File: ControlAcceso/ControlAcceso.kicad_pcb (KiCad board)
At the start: 2 copper layers, 53.3 x 61 mm, 12 parts

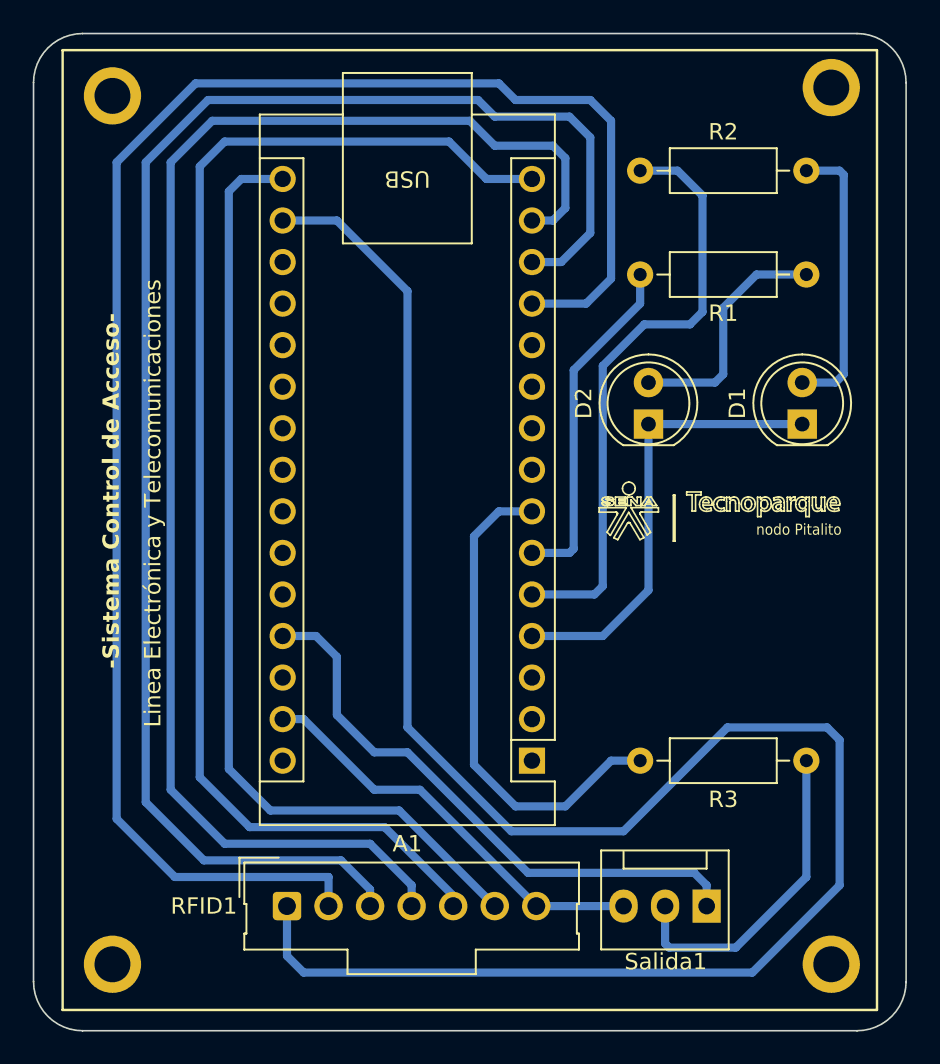
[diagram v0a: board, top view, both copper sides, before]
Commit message: Cambios Significativos
Se quito codigo de prueba, se cambio modulo RFID y se agrego  regulador 7805.
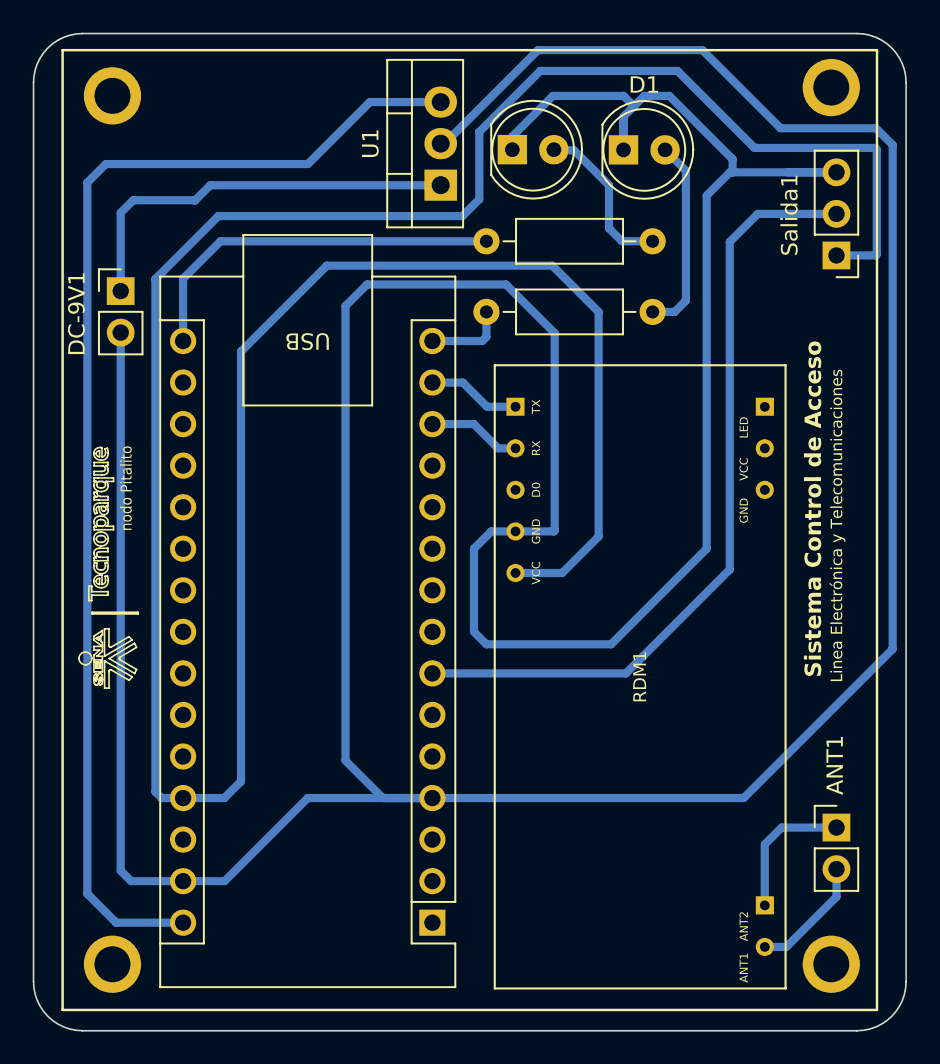
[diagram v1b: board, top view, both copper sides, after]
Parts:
- removed R3: 0, Resistor_THT:R_Axial_DIN0207_L6.3mm_D2.5mm_P10.16mm_Horizontal
- removed RFID1: Conn_01x07, Connector_Molex:Molex_SL_171971-0007_1x07_P2.54mm_Vertical
- added ANT1: Conn_01x02_Pin, Connector_PinHeader_2.54mm:PinHeader_1x02_P2.54mm_Vertical, F.Cu at (242.1, 84.1)
- added DC-9V1: Conn_01x02_Pin, Connector_PinHeader_2.54mm:PinHeader_1x02_P2.54mm_Vertical, F.Cu at (198.4, 51.3)
- added RDM1: RDM6300, RDM6300:RDM6300, F.Cu at (230.1, 74.9)
- added U1: LM7805_TO220, Package_TO_SOT_THT:TO-220-3_Vertical, F.Cu at (217.9, 44.8)
- Salida1: footprint Connector:FanPinHeader_1x03_P2.54mm_Vertical -> Connector_PinHeader_2.54mm:PinHeader_1x03_P2.54mm_Vertical
- moved Salida1 40.6 mm to (242.1, 49.1)
- moved D1 20.0 mm to (229.1, 42.7), turned to 0 degrees
- moved D2 18.7 mm to (222.3, 42.7), turned to 0 degrees
- moved R2 12.8 mm to (220.7, 52.6)
- moved A1 11.6 mm to (217.4, 89.9)
- moved R1 9.62 mm to (230.9, 48.3)
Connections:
- A1 pad 12: RST -> unconnected-(A1-D9-Pad12)
- A1 pad 13: SPI -> TX-SERIAL
- A1 pad 14: MOSI -> RX-SERIAL
- A1 pad 15: MISO -> LED-ON
- A1 pad 16: SCK -> LED-OFF
- A1 pad 5: LED-ON -> unconnected-(A1-D2-Pad5)
- A1 pad 6: LED-OFF -> unconnected-(A1-D3-Pad6)
- Salida1 pad 2: Net-(Salida1-Pin_2) -> OUT
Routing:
- net GND: track 53.4 -> 293.8 mm
- net +5V: track 35.6 -> 171.1 mm
- net 3V3: track 116.4 -> 0.00 mm
- net RST: track 104.6 -> 0.00 mm
- net SPI: track 95.9 -> 0.00 mm
- net MOSI: track 88.3 -> 0.00 mm
- net MISO: track 78.4 -> 0.00 mm
- net VIN: track 0.00 -> 73.5 mm
- net SCK: track 58.6 -> 0.00 mm
- net LED-ON: track 37.0 -> 4.93 mm
- net Net-(DC-9V1-Pin_1): track 0.00 -> 24.9 mm
- net Net-(Salida1-Pin_2): track 19.9 -> 0.00 mm
- net OUT: track 30.5 -> 48.1 mm
- net Net-(ANT1-Pin_1): track 0.00 -> 8.53 mm
- net Net-(ANT1-Pin_2): track 0.00 -> 7.34 mm
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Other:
- board text added: "Sistema Control de Acceso"
- board text removed: "-Sistema Control de Acceso-"

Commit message: Modificaciones Varias
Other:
- board text added: "+"
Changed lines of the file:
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@@
     (pad_to_mask_clearance 0)
     (pcbplotparams
-      (layerselection 0x00010fc_ffffffff)
+      (layerselection 0x0001000_ffffffff)
       (plot_on_all_layers_selection 0x0000000_00000000)
       (disableapertmacros false)
@@
       (net 25 "Net-(D2-A)") (pinfunction "A") (pintype "passive"))
     (model "${KICAD6_3DMODEL_DIR}/LED_THT.3dshapes/LED_D5.0mm.wrl"
-      (offset (xyz 0 0 0))
+      (offset (xyz 0 0 -3))
       (scale (xyz 1 1 1))
       (rotate (xyz 0 0 0))
@@
       (net 24 "Net-(D1-A)") (pinfunction "A") (pintype "passive"))
     (model "${KICAD6_3DMODEL_DIR}/LED_THT.3dshapes/LED_D5.0mm.wrl"
-      (offset (xyz 0 0 0))
+      (offset (xyz 0 0 -3))
       (scale (xyz 1 1 1))
       (rotate (xyz 0 0 0))
@@
     (pad "30" thru_hole oval (at 15.24 0 180) (size 1.6 1.6) (drill 1) (layers "*.Cu" "*.Mask")
       (net 23 "VIN") (pinfunction "VIN") (pintype "power_in"))
-    (model "C:/Users/hjest/Downloads/arduino-nano-33-iot-1.snapshot.3/Arduino Nano 33 IoT.stp"
-      (offset (xyz 7.5 -17.5 0.5))
+    (model "C:/Users/RED-TECNOPARQUE/Downloads/arduino-nano-33-iot-1.snapshot.3/Arduino Nano 33 IoT.stp"
+      (opacity 0.9900)      (offset (xyz 7.5 -17.5 1.5))
       (scale (xyz 1 1 1))
-      (rotate (xyz -90 0 0))
+      (rotate (xyz 90 -180 -180))
     )
   )
@@
     (pad "VCC1" thru_hole circle (at 13.97 7.62 90) (size 1.108 1.108) (drill 0.6) (layers "*.Cu" "*.Mask")
       (net 28 "unconnected-(RDM1-PadVCC1)") (pinfunction "VCC1") (pintype "bidirectional") (solder_mask_margin 0.102))
-    (model "C:/Users/hjest/Downloads/RDM6300/RDM6300.step"
-      (offset (xyz 0 0 5))
+    (model "C:/Users/RED-TECNOPARQUE/Downloads/rdm6300-4.snapshot.1/RDM6300.step"
+      (offset (xyz 0 0 4.5))
       (scale (xyz 1 1 1))
       (rotate (xyz 0 0 90))
@@
     (pad "3" thru_hole oval (at 5.08 0 90) (size 1.905 2) (drill 1.1) (layers "*.Cu" "*.Mask")
       (net 23 "VIN") (pinfunction "VO") (pintype "power_out"))
-    (model "C:/Users/hjest/Downloads/7805-3.snapshot.1/7805BC/7805BC.stp"
-      (offset (xyz 2.5 9 0.5))
+    (model "C:/Users/RED-TECNOPARQUE/Downloads/7805-3.snapshot.1/7805BC/7805BC.stp"
+      (offset (xyz 2.5 9 0))
       (scale (xyz 1 1 1))
       (rotate (xyz 0 0 0))
@@
     (effects (font (size 1 1) (thickness 0.2) bold) (justify left bottom))
   )
+  (gr_text "+\n" (at 199.42 49.26) (layer "F.SilkS")
+    (effects (font (size 1.5 1.5) (thickness 0.3) bold) (justify left bottom mirror))
+  )
   (gr_text "nodo Pitalito" (at 199.119622 65.980851 90) (layer "F.SilkS")
     (effects (font (size 0.677407 0.609666) (thickness 0.084675)) (justify left bottom))
@@
     (effects (font (size 0.7 0.7) (thickness 0.15)) (justify left bottom))
   )
+  (dimension (type aligned) (layer "User.1")
+    (pts (xy 235.36 35.6) (xy 235.4 96.58))
+    (height -24.775437)
+    (gr_text "60,9800 mm" (at 261.955432 66.072567 270.0375833) (layer "User.1")
+      (effects (font (size 1.5 1.5) (thickness 0.3)))
+    )
+    (format (prefix "") (suffix "") (units 3) (units_format 1) (precision 4))
+    (style (thickness 0.2) (arrow_length 1.27) (text_position_mode 0) (extension_height 0.58642) (extension_offset 0.5) keep_text_aligned)
+  )
+  (dimension (type aligned) (layer "User.1")
+    (pts (xy 246.38 38.56) (xy 193.04 38.56))
+    (height 8.87)
+    (gr_text "53,3400 mm" (at 219.71 27.89) (layer "User.1")
+      (effects (font (size 1.5 1.5) (thickness 0.3)))
+    )
+    (format (prefix "") (suffix "") (units 3) (units_format 1) (precision 4))
+    (style (thickness 0.2) (arrow_length 1.27) (text_position_mode 0) (extension_height 0.58642) (extension_offset 0.5) keep_text_aligned)
+  )
   (segment (start 223.874 36.576) (end 233.934 36.576) (width 0.5) (layer "B.Cu") (net 4))
